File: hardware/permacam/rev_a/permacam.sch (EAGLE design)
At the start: 95 parts, among them J1 TC2030-JLINK-NL, Q1 PMDXB950UPEL, Q2 PMDXB950UPEL, Q3 PMDXB950UPEL, Q4 PMDXB950UPEL, Q5 PMDXB950UPEL, Q6 PMDXB950UPEL, U1 AB1815-T3, U10 NRF52840, U2 BQ25505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

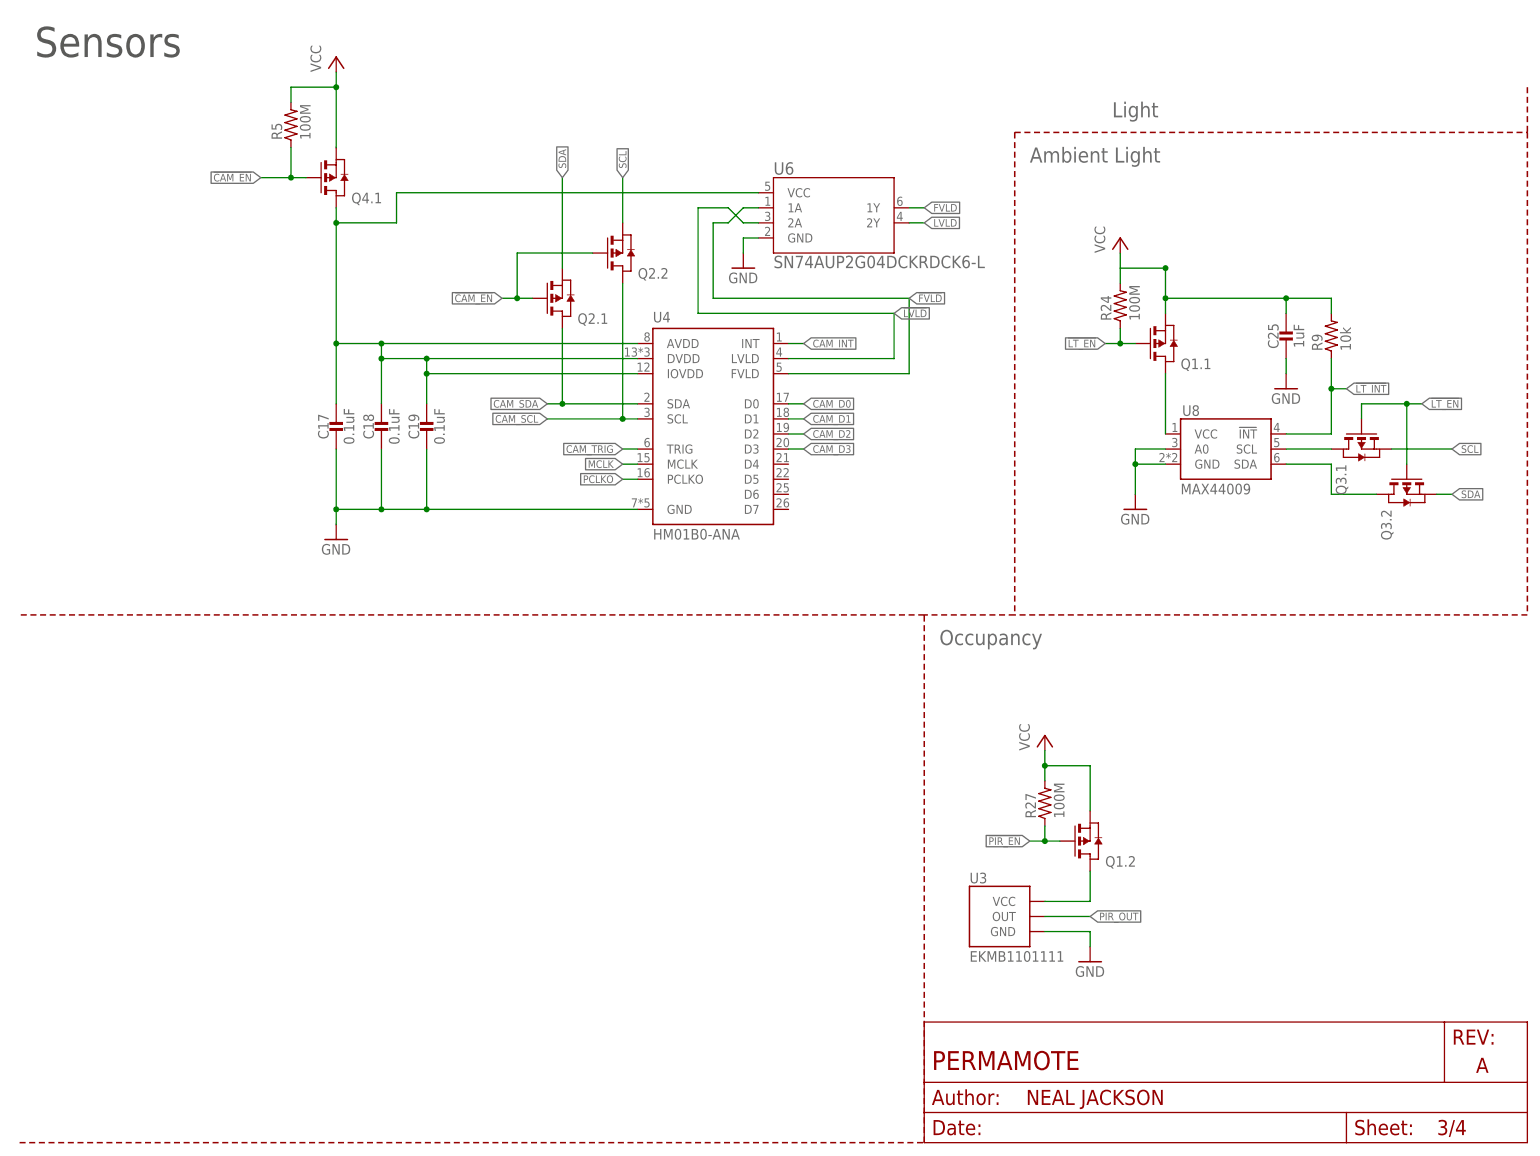
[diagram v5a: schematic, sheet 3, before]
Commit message: add debugging pads for camera signals
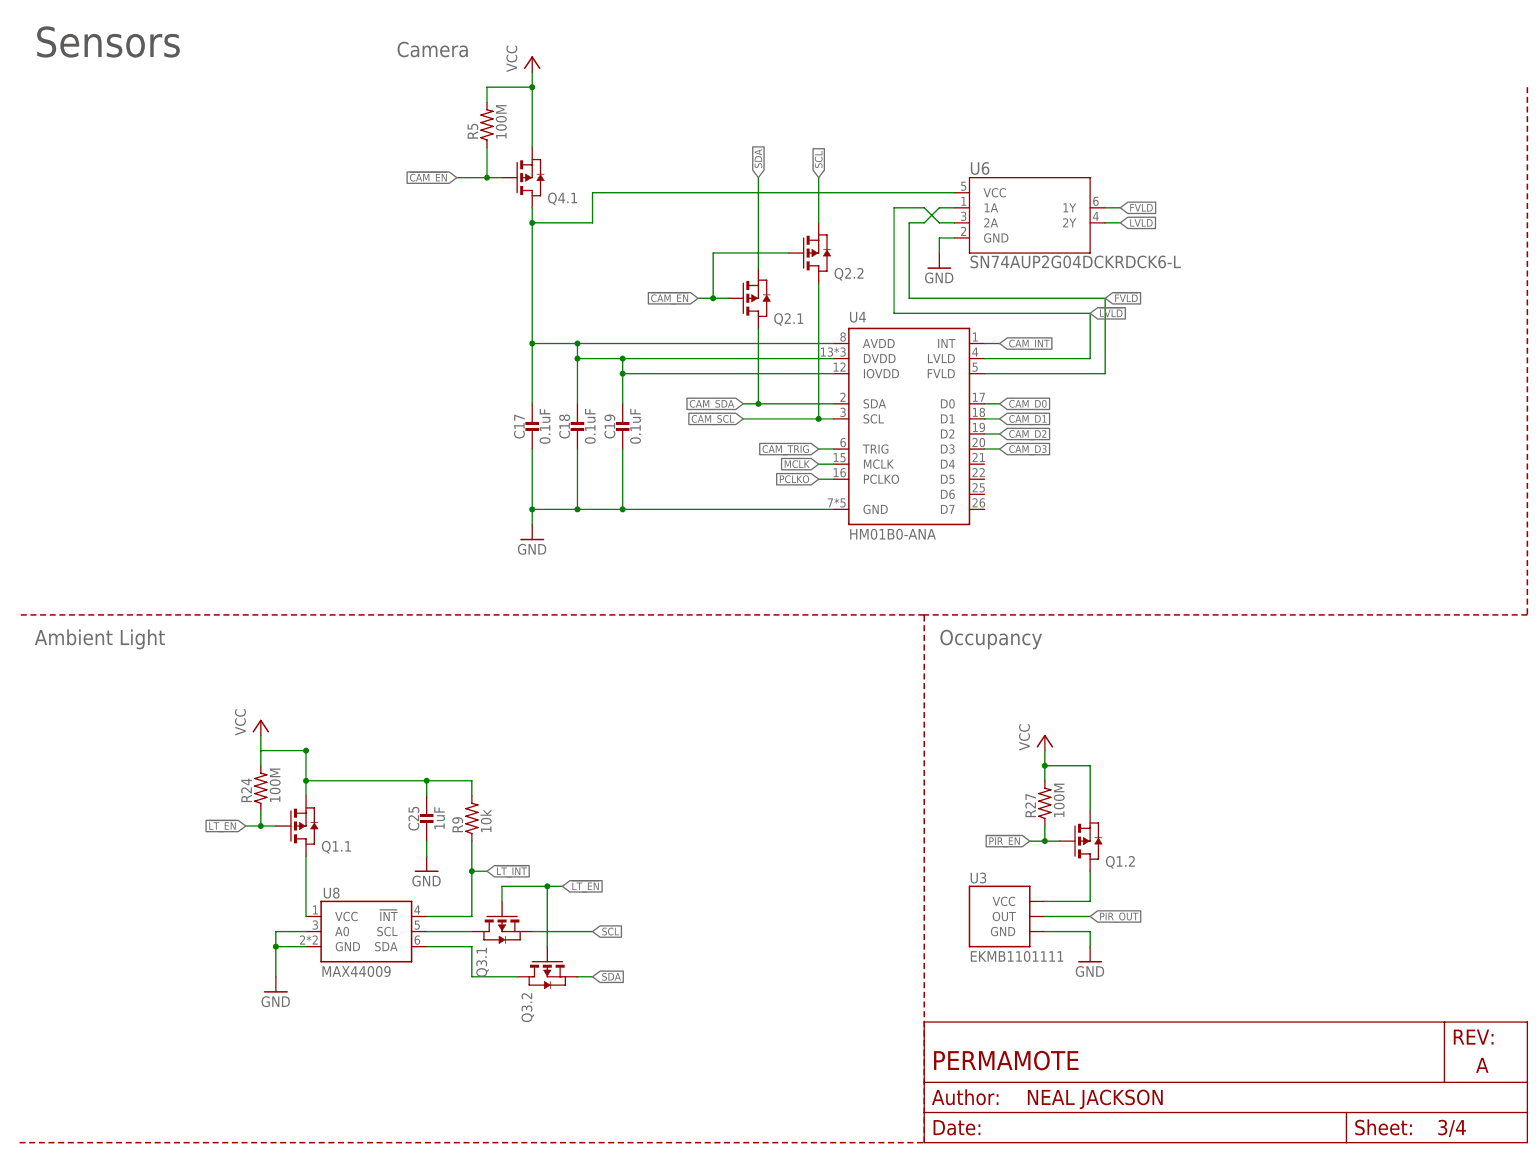
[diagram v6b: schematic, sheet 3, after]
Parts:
- added TP12, TP18, TP19, TP7, TP8, TP9: TEST-POINT, headers:TEST-POINT
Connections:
- net !FVLD: now also TP12.TESTPOINT
- net !LVLD: now also TP9.TESTPOINT
- net FVLD: now also TP8.TESTPOINT
- net LVLD: now also TP7.TESTPOINT
- net MCLK: now also TP19.TESTPOINT
- net PCLKO: now also TP18.TESTPOINT
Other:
- note added: "Camera"
- note removed: "Light"
- moved on the sheet: C17, C18, C19, C25, Q1.1, Q2.1, Q2.2, Q3.1, Q3.2, Q4.1, R24, R5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

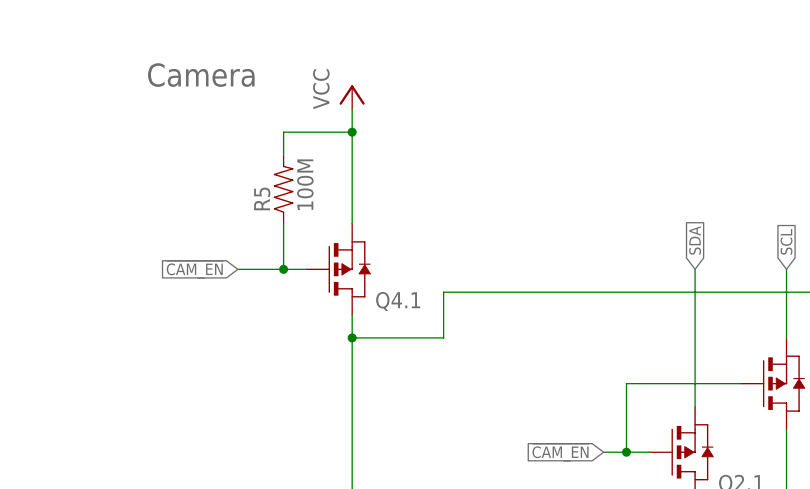
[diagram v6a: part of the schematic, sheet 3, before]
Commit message: Add decoupling cap for camera supply
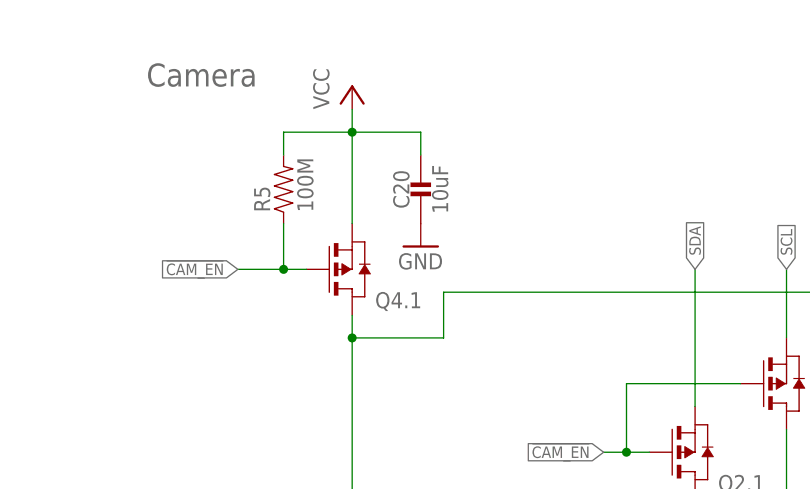
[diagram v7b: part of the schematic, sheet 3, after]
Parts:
- added C20: 10uF, passives:CAPACITOR0603_CAP
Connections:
- net GND: now also C20.2
- net VCC: now also C20.1
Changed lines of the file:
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@@
 <part name="TP18" library="headers" deviceset="TEST-POINT" device=""/>
 <part name="TP19" library="headers" deviceset="TEST-POINT" device=""/>
+<part name="C20" library="passives" deviceset="CAPACITOR" device="0603_CAP" value="10uF">
+<attribute name="DIGIKEY" value="490-3896-1-ND"/>
+<attribute name="MPN" value="GRM188R60J106ME47D "/>
+</part>
+<part name="GND15" library="supply1" library_urn="urn:adsk.eagle:library:371" deviceset="GND" device=""/>
 </parts>
 <sheets>
@@
 <attribute name="VALUE" x="82.042" y="168.91" size="1.778" layer="96" rot="R90"/>
 </instance>
+<instance part="C20" gate="G$1" x="93.98" y="172.72" smashed="yes">
+<attribute name="DIGIKEY" x="93.98" y="172.72" size="1.016" layer="96" align="bottom-center" display="off"/>
+<attribute name="MPN" x="93.98" y="172.72" size="1.778" layer="96" display="off"/>
+<attribute name="NAME" x="92.71" y="171.45" size="1.778" layer="95" ratio="12" rot="R90" align="bottom-center"/>
+<attribute name="VALUE" x="95.25" y="171.45" size="1.778" layer="96" ratio="12" rot="R270" align="bottom-center"/>
+</instance>
+<instance part="GND15" gate="1" x="93.98" y="165.1" smashed="yes">
+<attribute name="VALUE" x="91.44" y="162.56" size="1.778" layer="96"/>
+</instance>
 </instances>
 <busses>
@@
 <wire x1="157.48" y1="152.4" x2="154.94" y2="152.4" width="0.1524" layer="91"/>
 <wire x1="154.94" y1="152.4" x2="154.94" y2="149.86" width="0.1524" layer="91"/>
+</segment>
+<segment>
+<pinref part="C20" gate="G$1" pin="2"/>
+<pinref part="GND15" gate="1" pin="GND"/>
 </segment>
 </net>
@@
 <wire x1="78.74" y1="177.8" x2="86.36" y2="177.8" width="0.1524" layer="91"/>
 <junction x="86.36" y="177.8"/>
-</segment>
-</net>
+<pinref part="C20" gate="G$1" pin="1"/>
+<wire x1="86.36" y1="177.8" x2="93.98" y2="177.8" width="0.1524" layer="91"/>
+<wire x1="93.98" y1="177.8" x2="93.98" y2="175.26" width="0.1524" layer="91"/>
+</segment>
+</net>

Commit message: Implement will + josh changes
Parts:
- added R6, R7: DNP, passives:RESISTOR0402_RES
- added TP20, TP24, TP28, TP29: TEST-POINT, headers:TEST-POINT
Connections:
- net CAM_D0: now also TP20.TESTPOINT
- net CAM_D1: now also TP24.TESTPOINT
- net CAM_D2: now also TP28.TESTPOINT
- net CAM_D3: now also TP29.TESTPOINT
- net SCL: now also R7.1
- net SDA: now also R6.1
- net VCC: now also R6.2, R7.2
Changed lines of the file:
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@@
 </part>
 <part name="GND15" library="supply1" library_urn="urn:adsk.eagle:library:371" deviceset="GND" device=""/>
+<part name="TP20" library="headers" deviceset="TEST-POINT" device=""/>
+<part name="TP24" library="headers" deviceset="TEST-POINT" device=""/>
+<part name="TP28" library="headers" deviceset="TEST-POINT" device=""/>
+<part name="TP29" library="headers" deviceset="TEST-POINT" device=""/>
+<part name="R6" library="passives" deviceset="RESISTOR" device="0402_RES" value="DNP"/>
+<part name="R7" library="passives" deviceset="RESISTOR" device="0402_RES" value="DNP"/>
+<part name="P+6" library="supply1" library_urn="urn:adsk.eagle:library:371" deviceset="VCC" device=""/>
 </parts>
 <sheets>
@@
 <instance part="GND7" gate="1" x="91.44" y="48.26" smashed="yes">
 <attribute name="VALUE" x="88.9" y="45.72" size="1.778" layer="96"/>
+</instance>
+<instance part="R6" gate="G$1" x="78.74" y="109.22" smashed="yes" rot="R90">
+<attribute name="NAME" x="77.2414" y="105.41" size="1.778" layer="95" rot="R90"/>
+<attribute name="VALUE" x="82.042" y="105.41" size="1.778" layer="96" rot="R90"/>
+</instance>
+<instance part="R7" gate="G$1" x="86.36" y="109.22" smashed="yes" rot="R90">
+<attribute name="NAME" x="84.8614" y="105.41" size="1.778" layer="95" rot="R90"/>
+<attribute name="VALUE" x="89.662" y="105.41" size="1.778" layer="96" rot="R90"/>
+</instance>
+<instance part="P+6" gate="VCC" x="78.74" y="119.38" smashed="yes">
+<attribute name="VALUE" x="76.2" y="116.84" size="1.778" layer="96" rot="R90"/>
 </instance>
 </instances>
@@
 <pinref part="P+18" gate="VCC" pin="VCC"/>
 </segment>
+<segment>
+<pinref part="R6" gate="G$1" pin="2"/>
+<wire x1="78.74" y1="111.76" x2="78.74" y2="114.3" width="0.1524" layer="91"/>
+<wire x1="78.74" y1="114.3" x2="86.36" y2="114.3" width="0.1524" layer="91"/>
+<pinref part="R7" gate="G$1" pin="2"/>
+<wire x1="86.36" y1="114.3" x2="86.36" y2="111.76" width="0.1524" layer="91"/>
+<pinref part="P+6" gate="VCC" pin="VCC"/>
+<wire x1="78.74" y1="114.3" x2="78.74" y2="116.84" width="0.1524" layer="91"/>
+<junction x="78.74" y="114.3"/>
+</segment>
 </net>
 <net name="SCL" class="0">
 <segment>
-<label x="109.22" y="99.06" size="1.27" layer="95" rot="R180" xref="yes"/>
+<label x="76.2" y="99.06" size="1.27" layer="95" rot="R180" xref="yes"/>
 <pinref part="U10" gate="G$1" pin="P0.14"/>
-<wire x1="109.22" y1="99.06" x2="114.3" y2="99.06" width="0.1524" layer="91"/>
+<wire x1="76.2" y1="99.06" x2="86.36" y2="99.06" width="0.1524" layer="91"/>
+<pinref part="R7" gate="G$1" pin="1"/>
+<wire x1="86.36" y1="99.06" x2="114.3" y2="99.06" width="0.1524" layer="91"/>
+<wire x1="86.36" y1="104.14" x2="86.36" y2="99.06" width="0.1524" layer="91"/>
+<junction x="86.36" y="99.06"/>
 </segment>
 </net>
 <net name="SDA" class="0">
 <segment>
-<label x="109.22" y="101.6" size="1.27" layer="95" rot="R180" xref="yes"/>
+<label x="76.2" y="101.6" size="1.27" layer="95" rot="R180" xref="yes"/>
 <pinref part="U10" gate="G$1" pin="P0.13"/>
-<wire x1="109.22" y1="101.6" x2="114.3" y2="101.6" width="0.1524" layer="91"/>
+<wire x1="76.2" y1="101.6" x2="78.74" y2="101.6" width="0.1524" layer="91"/>
+<pinref part="R6" gate="G$1" pin="1"/>
+<wire x1="78.74" y1="101.6" x2="114.3" y2="101.6" width="0.1524" layer="91"/>
+<wire x1="78.74" y1="104.14" x2="78.74" y2="101.6" width="0.1524" layer="91"/>
+<junction x="78.74" y="101.6"/>
 </segment>
 </net>
@@
 <wire x1="180.34" y1="132.08" x2="180.34" y2="139.7" width="0.1524" layer="91"/>
 <wire x1="180.34" y1="139.7" x2="147.32" y2="139.7" width="0.1524" layer="91"/>
-<wire x1="147.32" y1="139.7" x2="147.32" y2="157.48" width="0.1524" layer="91"/>
-<wire x1="147.32" y1="157.48" x2="152.4" y2="157.48" width="0.1524" layer="91"/>
-<wire x1="152.4" y1="157.48" x2="154.94" y2="154.94" width="0.1524" layer="91"/>
+<wire x1="147.32" y1="139.7" x2="147.32" y2="154.94" width="0.1524" layer="91"/>
+<wire x1="147.32" y1="154.94" x2="152.4" y2="154.94" width="0.1524" layer="91"/>
+<wire x1="152.4" y1="154.94" x2="154.94" y2="154.94" width="0.1524" layer="91"/>
 <pinref part="U6" gate="A" pin="2A"/>
 <wire x1="157.48" y1="154.94" x2="154.94" y2="154.94" width="0.1524" layer="91"/>
@@
 <net name="!FVLD" class="0">
 <segment>
-<wire x1="149.86" y1="154.94" x2="149.86" y2="142.24" width="0.1524" layer="91"/>
+<wire x1="149.86" y1="157.48" x2="149.86" y2="142.24" width="0.1524" layer="91"/>
 <wire x1="149.86" y1="142.24" x2="182.88" y2="142.24" width="0.1524" layer="91"/>
 <wire x1="182.88" y1="142.24" x2="182.88" y2="129.54" width="0.1524" layer="91"/>
 <pinref part="U4" gate="G$1" pin="FVLD"/>
 <wire x1="182.88" y1="129.54" x2="162.56" y2="129.54" width="0.1524" layer="91"/>
-<wire x1="149.86" y1="154.94" x2="152.4" y2="154.94" width="0.1524" layer="91"/>
 <pinref part="U6" gate="A" pin="1A"/>
-<wire x1="157.48" y1="157.48" x2="154.94" y2="157.48" width="0.1524" layer="91"/>
-<wire x1="154.94" y1="157.48" x2="152.4" y2="154.94" width="0.1524" layer="91"/>
+<wire x1="157.48" y1="157.48" x2="149.86" y2="157.48" width="0.1524" layer="91"/>
 <label x="182.88" y="142.24" size="1.27" layer="95" xref="yes"/>
 </segment>
@@
 <attribute name="NAME" x="206.375" y="147.32" size="1.016" layer="95" ratio="12" rot="R180" align="center-right"/>
 </instance>
+<instance part="TP20" gate="G$1" x="203.2" y="157.48" smashed="yes" rot="R180">
+<attribute name="NAME" x="206.375" y="157.48" size="1.016" layer="95" ratio="12" rot="R180" align="center-right"/>
+</instance>
+<instance part="TP24" gate="G$1" x="203.2" y="154.94" smashed="yes" rot="R180">
+<attribute name="NAME" x="206.375" y="154.94" size="1.016" layer="95" ratio="12" rot="R180" align="center-right"/>
+</instance>
+<instance part="TP28" gate="G$1" x="203.2" y="152.4" smashed="yes" rot="R180">
+<attribute name="NAME" x="206.375" y="152.4" size="1.016" layer="95" ratio="12" rot="R180" align="center-right"/>
+</instance>
+<instance part="TP29" gate="G$1" x="203.2" y="149.86" smashed="yes" rot="R180">
+<attribute name="NAME" x="206.375" y="149.86" size="1.016" layer="95" ratio="12" rot="R180" align="center-right"/>
+</instance>
 </instances>
 <busses>
@@
 </segment>
 </net>
+<net name="CAM_D0" class="0">
+<segment>
+<wire x1="200.66" y1="157.48" x2="198.12" y2="157.48" width="0.1524" layer="91"/>
+<pinref part="TP20" gate="G$1" pin="TESTPOINT"/>
+<label x="198.12" y="157.48" size="1.27" layer="95" rot="R180" xref="yes"/>
+</segment>
+</net>
+<net name="CAM_D1" class="0">
+<segment>
+<wire x1="200.66" y1="154.94" x2="198.12" y2="154.94" width="0.1524" layer="91"/>
+<pinref part="TP24" gate="G$1" pin="TESTPOINT"/>
+<label x="198.12" y="154.94" size="1.27" layer="95" rot="R180" xref="yes"/>
+</segment>
+</net>
+<net name="CAM_D2" class="0">
+<segment>
+<wire x1="200.66" y1="152.4" x2="198.12" y2="152.4" width="0.1524" layer="91"/>
+<pinref part="TP28" gate="G$1" pin="TESTPOINT"/>
+<label x="198.12" y="152.4" size="1.27" layer="95" rot="R180" xref="yes"/>
+</segment>
+</net>
+<net name="CAM_D3" class="0">
+<segment>
+<wire x1="200.66" y1="149.86" x2="198.12" y2="149.86" width="0.1524" layer="91"/>
+<pinref part="TP29" gate="G$1" pin="TESTPOINT"/>
+<label x="198.12" y="149.86" size="1.27" layer="95" rot="R180" xref="yes"/>
+</segment>
+</net>
